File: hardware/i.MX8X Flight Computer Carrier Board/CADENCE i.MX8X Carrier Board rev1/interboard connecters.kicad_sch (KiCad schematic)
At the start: 61 parts, among them CN2 DF11-16DP-2DSA(08), CN3 DF11-16DP-2DSA(08), CN4 DF11-16DP-2DSA(08), J10 Conn_01x04, J11 Conn_01x04, J12 Conn_01x04, J13 Conn_01x04, J14 Conn_01x04, J15 Conn_01x04, J16 Conn_01x04, J17 Conn_01x04, J18 Conn_01x04, J19 Conn_01x04, J20 Conn_01x04, J21 Conn_01x04, J22 Conn_01x04, J23 Conn_01x04, J24 Conn_02x02_Odd_Even, J25 Conn_01x04, J26 Conn_01x04, J27 Conn_01x04, J28 Conn_01x05, J29 Conn_01x05, J30 Conn_02x18_Odd_Even, J31 Conn_01x04, J32 Conn_01x05, J33 Conn_01x05, J6 Conn_01x01, J7 Conn_01x08, J8 Conn_02x26_Odd_Even, J9 Conn_02x26_Odd_Even, U36 SN65HVD233, U37 INA219AxDCN, U38 TPS22810DBV, U39 INA219AxDCN, U40 TPS22810DBV, U41 INA219AxDCN, U42 TPS22975

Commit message: Check GPIO connection is the correct version
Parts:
- C141, C142: footprint Capacitor_SMD:C_0603_1608Metric -> Capacitor_SMD:C_0805_2012Metric
- J7: footprint (none) -> Footprints:CONN_BM08B-SRSS-TBLFSN_JST
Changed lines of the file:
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@@
 			)
 		)
-		(property "Footprint" "Capacitor_SMD:C_0603_1608Metric"
+		(property "Footprint" "Capacitor_SMD:C_0805_2012Metric"
 			(at 364.7948 226.06 0)
 			(effects
@@
 			)
 		)
-		(property "Footprint" "Capacitor_SMD:C_0603_1608Metric"
+		(property "Footprint" "Capacitor_SMD:C_0805_2012Metric"
 			(at 373.6848 226.06 0)
 			(effects
@@
 			)
 		)
-		(property "Footprint" ""
+		(property "Footprint" "Footprints:CONN_BM08B-SRSS-TBLFSN_JST"
 			(at 55.88 68.58 0)
 			(effects
@@
 			)
 		)
-		(property "Datasheet" "~"
+		(property "Datasheet" "https://www.digikey.com/en/products/detail/jst-sales-america-inc/BM08B-SRSS-TB/926700?msockid=1552b9517fec6f0231b8aa377e686e58"
 			(at 55.88 68.58 0)
 			(effects

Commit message: updated footprints
- shunt resistor for sense
footprint checks
- resolved mux footprint issue

to do:
-imx8x som footprint
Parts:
- R176, R178, R180: footprint Resistor_SMD:R_0402_1005Metric -> Footprints:RES_WSHM2818_VIS
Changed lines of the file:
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@@
 			)
 		)
-		(property "Footprint" "Resistor_SMD:R_0402_1005Metric"
+		(property "Footprint" "Footprints:RES_WSHM2818_VIS"
 			(at 115.062 106.68 90)
 			(effects
@@
 			)
 		)
-		(property "Footprint" "Resistor_SMD:R_0402_1005Metric"
+		(property "Footprint" "Footprints:RES_WSHM2818_VIS"
 			(at 318.262 198.12 90)
 			(effects
@@
 			)
 		)
-		(property "Footprint" "Resistor_SMD:R_0402_1005Metric"
+		(property "Footprint" "Footprints:RES_WSHM2818_VIS"
 			(at 168.402 262.89 90)
 			(effects

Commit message: more layout changes
- finished microSD layout, payload connector, and some other peripheral layouts but it got messed up when grouping & i didnt notice so yay (i wasted my time)
- 3.3v buck completed
-replaced satnogs connector footprint
-resized board
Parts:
- J8, J9: footprint Connector_PinHeader_2.54mm:PinHeader_2x26_P2.54mm_Vertical -> Footprints:ESQ-126-39-x-D
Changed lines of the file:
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@@
 			)
 		)
-		(property "Footprint" "Connector_PinHeader_2.54mm:PinHeader_2x26_P2.54mm_Vertical"
+		(property "Footprint" "Footprints:ESQ-126-39-x-D"
 			(at 87.63 243.84 0)
 			(effects
@@
 			)
 		)
-		(property "Footprint" "Connector_PinHeader_2.54mm:PinHeader_2x26_P2.54mm_Vertical"
+		(property "Footprint" "Footprints:ESQ-126-39-x-D"
 			(at 129.54 243.84 0)
 			(effects

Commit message: peripheral & connector layout update
- finished rs-422 payload connector layout (changed footprint, package being used has around 40 left in stock at JLCPCB)
- modified memory (mram & nor flash) ic layouts & organized into layout blocks for easy placement later
- revised & reorganized gps, rtc, temp sensor, imu connections into separate layout  blocks. also moved around gps and moved peripherals into completed layout circuit block section for later placement
- changed some power monitor shunt resistor footprints so 10W or so doesnt go thru a sad 0402 resistor lol
- fixed microSD connection issues
- adjusted gps 50 ohm coax impedance connection (28 ohm trace + 22ohm resistor)
- 50 ohm impedance calculations for gps added to schematic & disclaimer for switching regulator low ripple burst mode added to power schematic page

to do:
- verify that board power monitor wont lead to reverse current driving i.mx8x and make it explode
- look further into & verify that cmos image sensor connector is correct one being used by lucid
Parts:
- renumbered R174 to R152, R175 to R153, R176 to R154, R177 to R155, R178 to R156, R179 to R157, R180 to R158, TP22 to TP24, TP23 to TP25
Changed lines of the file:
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@@
 		(on_board yes)
 		(dnp no)
-		(property "Reference" "R177"
+		(property "Reference" "R155"
 			(at 155.956 69.596 90)
 			(effects
@@
 			(project "CADENCE i.MX8X Carrier Board rev1"
 				(path "/de284495-d382-47cb-b528-76e440980d40/912a7967-b8a7-4e29-8c0b-8042b13af5ba"
-					(reference "R177")
+					(reference "R155")
 					(unit 1)
 				)
@@
 		(on_board yes)
 		(dnp no)
-		(property "Reference" "#FLG031"
+		(property "Reference" "#FLG029"
 			(at 323.215 238.76 0)
 			(effects
@@
 			(project "CADENCE i.MX8X Carrier Board rev1"
 				(path "/de284495-d382-47cb-b528-76e440980d40/912a7967-b8a7-4e29-8c0b-8042b13af5ba"
-					(reference "#FLG031")
+					(reference "#FLG029")
 					(unit 1)
 				)
@@
 		(on_board yes)
 		(dnp no)
-		(property "Reference" "R176"
+		(property "Reference" "R154"
 			(at 119.38 105.4099 0)
 			(effects
@@
 			(project "CADENCE i.MX8X Carrier Board rev1"
 				(path "/de284495-d382-47cb-b528-76e440980d40/912a7967-b8a7-4e29-8c0b-8042b13af5ba"
-					(reference "R176")
+					(reference "R154")
 					(unit 1)
 				)
@@
 		(on_board yes)
 		(dnp no)
-		(property "Reference" "R174"
+		(property "Reference" "R152"
 			(at 45.974 223.012 0)
 			(effects
@@
 			(project "CADENCE i.MX8X Carrier Board rev1"
 				(path "/de284495-d382-47cb-b528-76e440980d40/912a7967-b8a7-4e29-8c0b-8042b13af5ba"
-					(reference "R174")
+					(reference "R152")
 					(unit 1)
 				)
@@
 		(dnp no)
 		(fields_autoplaced yes)
-		(property "Reference" "#FLG032"
+		(property "Reference" "#FLG030"
 			(at 379.73 184.785 0)
 			(effects
@@
 			(project "CADENCE i.MX8X Carrier Board rev1"
 				(path "/de284495-d382-47cb-b528-76e440980d40/912a7967-b8a7-4e29-8c0b-8042b13af5ba"
-					(reference "#FLG032")
+					(reference "#FLG030")
 					(unit 1)
 				)
@@
 		(on_board yes)
 		(dnp no)
-		(property "Reference" "R179"
+		(property "Reference" "R157"
 			(at 224.536 210.566 90)
 			(effects
@@
 			(project "CADENCE i.MX8X Carrier Board rev1"
 				(path "/de284495-d382-47cb-b528-76e440980d40/912a7967-b8a7-4e29-8c0b-8042b13af5ba"
-					(reference "R179")
+					(reference "R157")
 					(unit 1)
 				)
@@
 		(on_board yes)
 		(dnp no)
-		(property "Reference" "R180"
+		(property "Reference" "R158"
 			(at 322.58 196.8499 0)
 			(effects
@@
 			(project "CADENCE i.MX8X Carrier Board rev1"
 				(path "/de284495-d382-47cb-b528-76e440980d40/912a7967-b8a7-4e29-8c0b-8042b13af5ba"
-					(reference "R180")
+					(reference "R158")
 					(unit 1)
 				)
@@
 		(on_board yes)
 		(dnp no)
-		(property "Reference" "R175"
+		(property "Reference" "R153"
 			(at 70.104 209.55 0)
 			(effects
@@
 			(project "CADENCE i.MX8X Carrier Board rev1"
 				(path "/de284495-d382-47cb-b528-76e440980d40/912a7967-b8a7-4e29-8c0b-8042b13af5ba"
-					(reference "R175")
+					(reference "R153")
 					(unit 1)
 				)
@@
 		(on_board yes)
 		(dnp no)
-		(property "Reference" "TP23"
+		(property "Reference" "TP25"
 			(at 142.24 221.234 90)
 			(effects
@@
 			(project "CADENCE i.MX8X Carrier Board rev1"
 				(path "/de284495-d382-47cb-b528-76e440980d40/912a7967-b8a7-4e29-8c0b-8042b13af5ba"
-					(reference "TP23")
+					(reference "TP25")
 					(unit 1)
 				)
@@
 		(on_board yes)
 		(dnp no)
-		(property "Reference" "TP22"
+		(property "Reference" "TP24"
 			(at 111.76 110.744 90)
 			(effects
@@
 			(project "CADENCE i.MX8X Carrier Board rev1"
 				(path "/de284495-d382-47cb-b528-76e440980d40/912a7967-b8a7-4e29-8c0b-8042b13af5ba"
-					(reference "TP22")
+					(reference "TP24")
 					(unit 1)
 				)
@@
 		(on_board yes)
 		(dnp no)
-		(property "Reference" "R178"
+		(property "Reference" "R156"
 			(at 172.72 261.6199 0)
 			(effects
@@
 			(project "CADENCE i.MX8X Carrier Board rev1"
 				(path "/de284495-d382-47cb-b528-76e440980d40/912a7967-b8a7-4e29-8c0b-8042b13af5ba"
-					(reference "R178")
+					(reference "R156")
 					(unit 1)
 				)

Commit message: layout block placement
started placing components onto board itself
-satnogs power monitor and connector reoriented
-m3 mounting holes will be added to corners
- nor flash, mrams added under the som on top layer
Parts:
- added H1, H2, H3, H4: MountingHole, MountingHole:MountingHole_3.2mm_M3, symbol Mechanical:MountingHole
- added H5, H6: MountingHole, MountingHole:MountingHole_2.7mm_M2.5, symbol Mechanical:MountingHole
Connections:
- net CAN-: now reaches J8.1 (Pin_1), R153.2, U36.6 (CANL)
- net CAN+: now reaches J8.3 (Pin_3), R153.1, U36.7 (CANH)
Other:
- note added: "M3 Mounting Holes"
- note added: "WSHP28182L000FEA"
- note added: "i.MX8X SOM Mounting Holes"

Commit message: layout update
- removed vbus regulators (left vbus unconnected for now, will reconnect to vbus on som later)
- outbound signal connectors to adcs & ebyte placement with i2c buffers and power monitors, etc
- layout block placement and some connections
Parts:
- renumbered C130 to C126, C131 to C127, C132 to C128, C133 to C129, C134 to C130, C135 to C131, C136 to C132, C137 to C133, C138 to C134, C139 to C135, C140 to C136, C141 to C137, C142 to C138, C143 to C139, TP24 to TP22, TP25 to TP23, U36 to U34, U37 to U35, U38 to U36, U39 to U37, U40 to U38, U41 to U39, U42 to U40

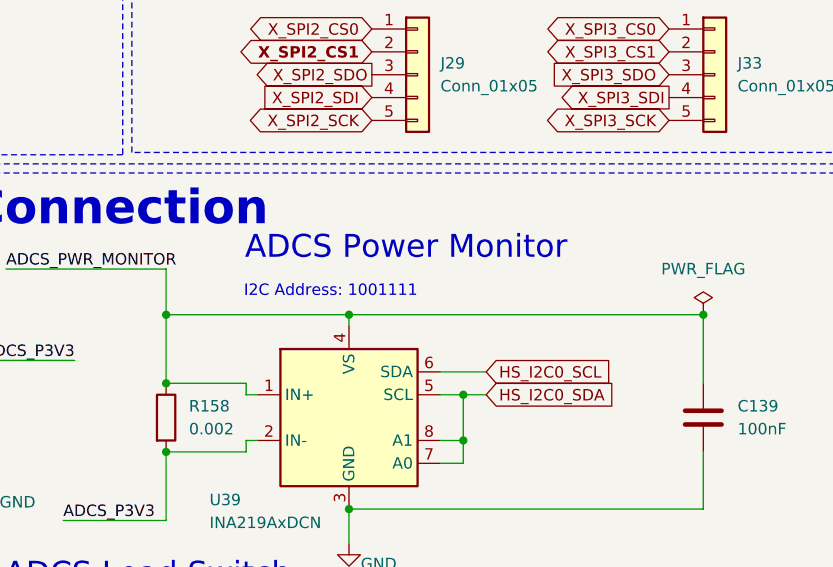
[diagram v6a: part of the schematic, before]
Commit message: layout connections
- payload rs-422 completed
- fixed some power net names
- can bus to satnogs
- gps uart
- ftdi uart
- spi & octal spi to memories
- microsd
- more digital signal connections
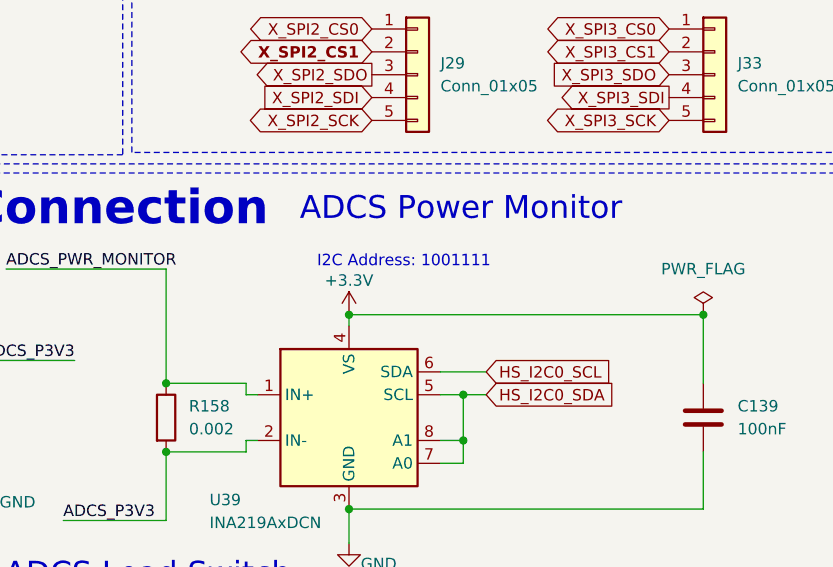
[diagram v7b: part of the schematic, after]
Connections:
- net +3.3V: now also C139.1, U39.4 (VS)
- net ADCS_PWR_MONITOR: no longer C139.1, U39.4 (VS)
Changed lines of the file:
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@@
 	(text "ADCS Power Monitor"
 		(exclude_from_sim no)
-		(at 346.71 179.324 0)
+		(at 352.806 175.006 0)
 		(effects
 			(font
@@
 	(text "I2C Address: 1001111"
 		(exclude_from_sim no)
-		(at 338.328 184.15 0)
+		(at 346.456 180.848 0)
 		(effects
 			(font
@@
 	)
 	(junction
-		(at 320.04 186.69)
-		(diameter 0)
-		(color 0 0 0 0)
-	)
-	(junction
 		(at 135.89 118.11)
 		(diameter 0)
@@
 	(wire
 		(pts
-			(xy 320.04 181.61) (xy 320.04 186.69)
+			(xy 320.04 181.61) (xy 320.04 194.31)
 		)
 		(stroke
@@
 	(wire
 		(pts
-			(xy 320.04 186.69) (xy 320.04 194.31)
-		)
-		(stroke
-			(width 0)
-			(type default)
-		)
-	)
-	(wire
-		(pts
 			(xy 125.73 104.14) (xy 125.73 102.87)
 		)
@@
 	(wire
 		(pts
-			(xy 320.04 186.69) (xy 340.36 186.69)
-		)
-		(stroke
-			(width 0)
-			(type default)
-		)
-	)
-	(wire
-		(pts
 			(xy 34.29 215.9) (xy 46.99 215.9)
 		)
@@
 					(unit 1)
 				)
+			)
+		)
+	)
+	(symbol
+		(lib_id "power:+3.3V")
+		(at 340.36 186.69 0)
+		(unit 1)
+		(exclude_from_sim no)
+		(in_bom yes)
+		(on_board yes)
+		(dnp no)
+		(property "Reference" "#PWR073"
+			(at 340.36 190.5 0)
+			(effects
+				(font
+					(size 1.27 1.27)
+				)
+				(hide yes)
+			)
+		)
+		(property "Value" "+3.3V"
+			(at 340.36 182.88 0)
+			(effects
+				(font
+					(size 1.27 1.27)
+				)
+			)
+		)
+		(property "Footprint" ""
+			(at 340.36 186.69 0)
+			(effects
+				(font
+					(size 1.27 1.27)
+				)
+				(hide yes)
+			)
+		)
+		(property "Datasheet" ""
+			(at 340.36 186.69 0)
+			(effects
+				(font
+					(size 1.27 1.27)
+				)
+				(hide yes)
+			)
+		)
+		(property "Description" "Power symbol creates a global label with name \"+3.3V\""
+			(at 340.36 186.69 0)
+			(effects
+				(font
+					(size 1.27 1.27)
+				)
+				(hide yes)
+			)
+		)
+		(pin "1"
+		)
+		(instances
+			(project "CADENCE i.MX8X Carrier Board rev1"
+				(path "/de284495-d382-47cb-b528-76e440980d40/912a7967-b8a7-4e29-8c0b-8042b13af5ba"
+					(reference "#PWR073")
+					(unit 1)
+				)

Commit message: changes to debug footprints
changed most debugs to 1.27mm headers instead of 2.54mm
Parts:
- J10, J11, J12, J13, J14, J15, J16, J17, J18, J19, J20, J21, J22, J23, J25, J26, J27, J31: footprint Connector_PinHeader_2.54mm:PinHeader_1x04_P2.54mm_Vertical -> Connector_PinHeader_1.27mm:PinHeader_1x04_P1.27mm_Vertical
- J28, J29, J32, J33: footprint Connector_PinHeader_2.54mm:PinHeader_1x05_P2.54mm_Vertical -> Connector_PinHeader_1.27mm:PinHeader_1x05_P1.27mm_Vertical
- J30: footprint Connector_PinHeader_2.54mm:PinHeader_2x18_P2.54mm_Vertical -> Connector_PinHeader_1.27mm:PinHeader_2x18_P1.27mm_Vertical
- J6: footprint Connector_PinHeader_2.54mm:PinHeader_1x01_P2.54mm_Vertical -> Connector_PinHeader_1.00mm:PinHeader_1x01_P1.00mm_Vertical
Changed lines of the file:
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@@
 			)
 		)
-		(property "Footprint" "Connector_PinHeader_2.54mm:PinHeader_1x04_P2.54mm_Vertical"
+		(property "Footprint" "Connector_PinHeader_1.27mm:PinHeader_1x04_P1.27mm_Vertical"
 			(at 229.87 88.9 0)
 			(effects
@@
 			)
 		)
-		(property "Footprint" "Connector_PinHeader_2.54mm:PinHeader_1x04_P2.54mm_Vertical"
+		(property "Footprint" "Connector_PinHeader_1.27mm:PinHeader_1x04_P1.27mm_Vertical"
 			(at 281.94 41.91 0)
 			(effects
@@
 			)
 		)
-		(property "Footprint" "Connector_PinHeader_2.54mm:PinHeader_1x04_P2.54mm_Vertical"
+		(property "Footprint" "Connector_PinHeader_1.27mm:PinHeader_1x04_P1.27mm_Vertical"
 			(at 269.24 106.68 0)
 			(effects
@@
 			)
 		)
-		(property "Footprint" "Connector_PinHeader_2.54mm:PinHeader_1x05_P2.54mm_Vertical"
+		(property "Footprint" "Connector_PinHeader_1.27mm:PinHeader_1x05_P1.27mm_Vertical"
 			(at 381 160.02 0)
 			(effects
@@
 			)
 		)
-		(property "Footprint" "Connector_PinHeader_2.54mm:PinHeader_1x04_P2.54mm_Vertical"
+		(property "Footprint" "Connector_PinHeader_1.27mm:PinHeader_1x04_P1.27mm_Vertical"
 			(at 233.68 41.91 0)
 			(effects
@@
 			)
 		)
-		(property "Footprint" "Connector_PinHeader_2.54mm:PinHeader_1x04_P2.54mm_Vertical"
+		(property "Footprint" "Connector_PinHeader_1.27mm:PinHeader_1x04_P1.27mm_Vertical"
 			(at 234.95 58.42 0)
 			(effects
@@
 			)
 		)
-		(property "Footprint" "Connector_PinHeader_2.54mm:PinHeader_1x04_P2.54mm_Vertical"
+		(property "Footprint" "Connector_PinHeader_1.27mm:PinHeader_1x04_P1.27mm_Vertical"
 			(at 219.71 151.13 0)
 			(effects
@@
 			)
 		)
-		(property "Footprint" "Connector_PinHeader_2.54mm:PinHeader_1x04_P2.54mm_Vertical"
+		(property "Footprint" "Connector_PinHeader_1.27mm:PinHeader_1x04_P1.27mm_Vertical"
 			(at 281.94 58.42 0)
 			(effects
@@
 			)
 		)
-		(property "Footprint" "Connector_PinHeader_2.54mm:PinHeader_1x04_P2.54mm_Vertical"
+		(property "Footprint" "Connector_PinHeader_1.27mm:PinHeader_1x04_P1.27mm_Vertical"
 			(at 226.06 132.08 0)
 			(effects
@@
 			)
 		)
-		(property "Footprint" "Connector_PinHeader_2.54mm:PinHeader_1x04_P2.54mm_Vertical"
+		(property "Footprint" "Connector_PinHeader_1.27mm:PinHeader_1x04_P1.27mm_Vertical"
 			(at 264.16 132.08 0)
 			(effects
@@
 			)
 		)
-		(property "Footprint" "Connector_PinHeader_2.54mm:PinHeader_1x04_P2.54mm_Vertical"
+		(property "Footprint" "Connector_PinHeader_1.27mm:PinHeader_1x04_P1.27mm_Vertical"
 			(at 264.16 149.86 0)
 			(effects
@@
 			)
 		)
-		(property "Footprint" "Connector_PinHeader_2.54mm:PinHeader_1x05_P2.54mm_Vertical"
+		(property "Footprint" "Connector_PinHeader_1.27mm:PinHeader_1x05_P1.27mm_Vertical"
 			(at 347.98 160.02 0)
 			(effects
@@
 			)
 		)
-		(property "Footprint" "Connector_PinHeader_2.54mm:PinHeader_1x04_P2.54mm_Vertical"
+		(property "Footprint" "Connector_PinHeader_1.27mm:PinHeader_1x04_P1.27mm_Vertical"
 			(at 209.55 41.91 0)
 			(effects
@@
 			)
 		)
-		(property "Footprint" "Connector_PinHeader_2.54mm:PinHeader_1x04_P2.54mm_Vertical"
+		(property "Footprint" "Connector_PinHeader_1.27mm:PinHeader_1x04_P1.27mm_Vertical"
 			(at 269.24 88.9 0)
 			(effects
@@
 			)
 		)
-		(property "Footprint" "Connector_PinHeader_2.54mm:PinHeader_1x04_P2.54mm_Vertical"
+		(property "Footprint" "Connector_PinHeader_1.27mm:PinHeader_1x04_P1.27mm_Vertical"
 			(at 229.87 106.68 0)
 			(effects
@@
 			)
 		)
-		(property "Footprint" "Connector_PinHeader_2.54mm:PinHeader_1x05_P2.54mm_Vertical"
+		(property "Footprint" "Connector_PinHeader_1.27mm:PinHeader_1x05_P1.27mm_Vertical"
 			(at 347.98 142.24 0)
 			(effects
@@
 			)
 		)
-		(property "Footprint" "Connector_PinHeader_2.54mm:PinHeader_1x05_P2.54mm_Vertical"
+		(property "Footprint" "Connector_PinHeader_1.27mm:PinHeader_1x05_P1.27mm_Vertical"
 			(at 381 142.24 0)
 			(effects
@@
 			)
 		)
-		(property "Footprint" "Connector_PinHeader_2.54mm:PinHeader_2x18_P2.54mm_Vertical"
+		(property "Footprint" "Connector_PinHeader_1.27mm:PinHeader_2x18_P1.27mm_Vertical"
 			(at 351.79 67.31 0)
 			(effects
@@
 			)
 		)
-		(property "Footprint" "Connector_PinHeader_2.54mm:PinHeader_1x04_P2.54mm_Vertical"
+		(property "Footprint" "Connector_PinHeader_1.27mm:PinHeader_1x04_P1.27mm_Vertical"
 			(at 300.99 132.08 0)
 			(effects
@@
 			)
 		)
-		(property "Footprint" "Connector_PinHeader_2.54mm:PinHeader_1x01_P2.54mm_Vertical"
+		(property "Footprint" "Connector_PinHeader_1.00mm:PinHeader_1x01_P1.00mm_Vertical"
 			(at 34.29 220.98 0)
 			(effects
@@
 			)
 		)
-		(property "Footprint" "Connector_PinHeader_2.54mm:PinHeader_1x04_P2.54mm_Vertical"
+		(property "Footprint" "Connector_PinHeader_1.27mm:PinHeader_1x04_P1.27mm_Vertical"
 			(at 259.08 58.42 0)
 			(effects
@@
 			)
 		)
-		(property "Footprint" "Connector_PinHeader_2.54mm:PinHeader_1x04_P2.54mm_Vertical"
+		(property "Footprint" "Connector_PinHeader_1.27mm:PinHeader_1x04_P1.27mm_Vertical"
 			(at 209.55 58.42 0)
 			(effects
@@
 			)
 		)
-		(property "Footprint" "Connector_PinHeader_2.54mm:PinHeader_1x04_P2.54mm_Vertical"
+		(property "Footprint" "Connector_PinHeader_1.27mm:PinHeader_1x04_P1.27mm_Vertical"
 			(at 377.19 107.95 0)
 			(effects
@@
 			)
 		)
-		(property "Footprint" "Connector_PinHeader_2.54mm:PinHeader_1x04_P2.54mm_Vertical"
+		(property "Footprint" "Connector_PinHeader_1.27mm:PinHeader_1x04_P1.27mm_Vertical"
 			(at 257.81 41.91 0)
 			(effects
